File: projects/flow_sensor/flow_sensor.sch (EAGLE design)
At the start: 92 parts, among them IC1 TPS61200, IC2 TPS61200, IC3 MIC5219BM5, J5 455-1750-1-ND

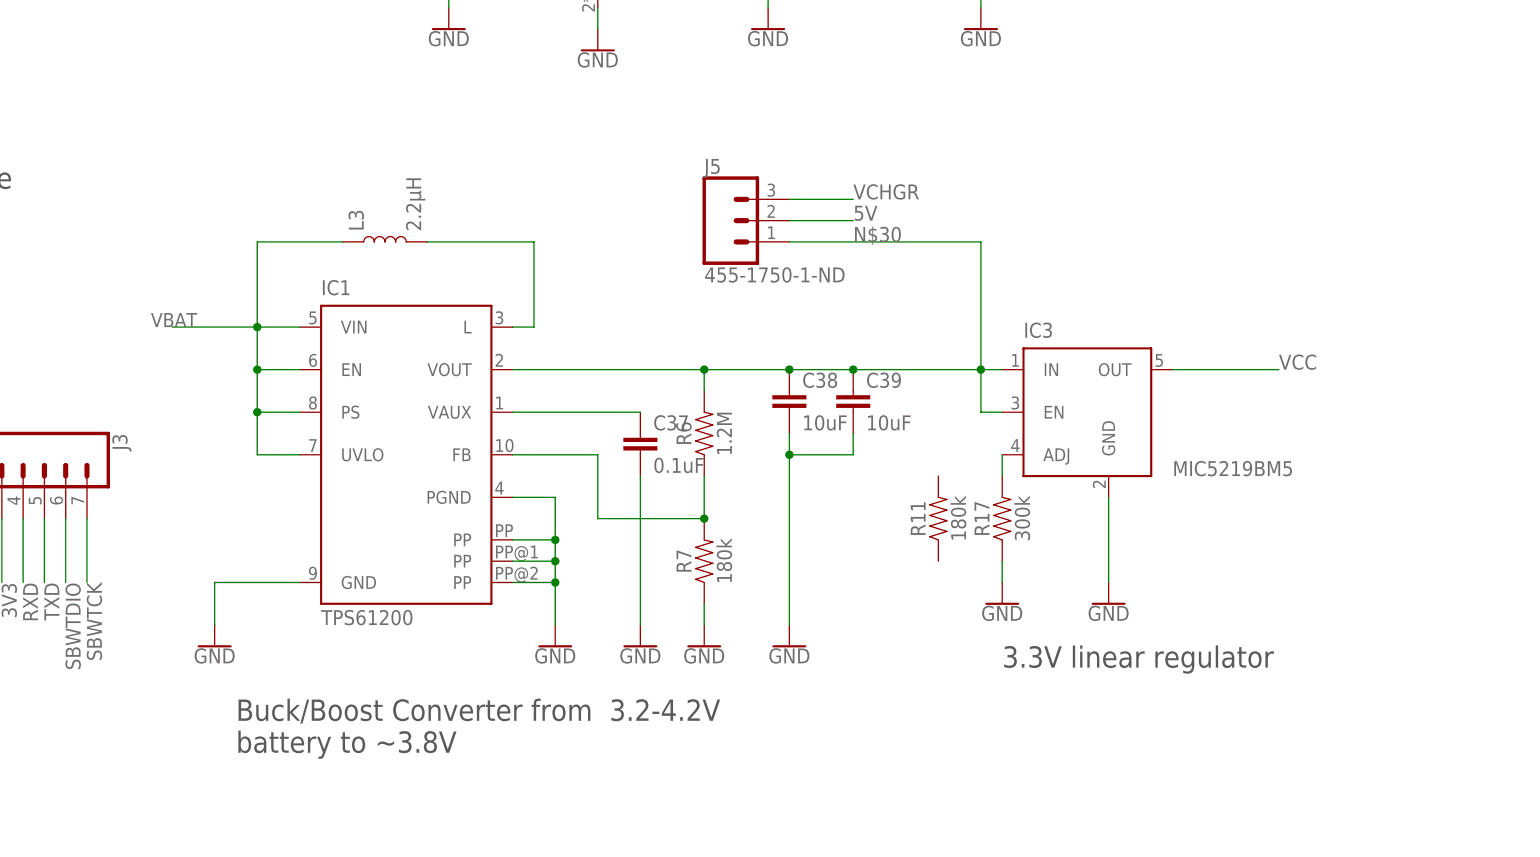
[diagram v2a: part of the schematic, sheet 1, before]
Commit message: Added MAX1726 linear regulator and replaced circuit-side boost converter
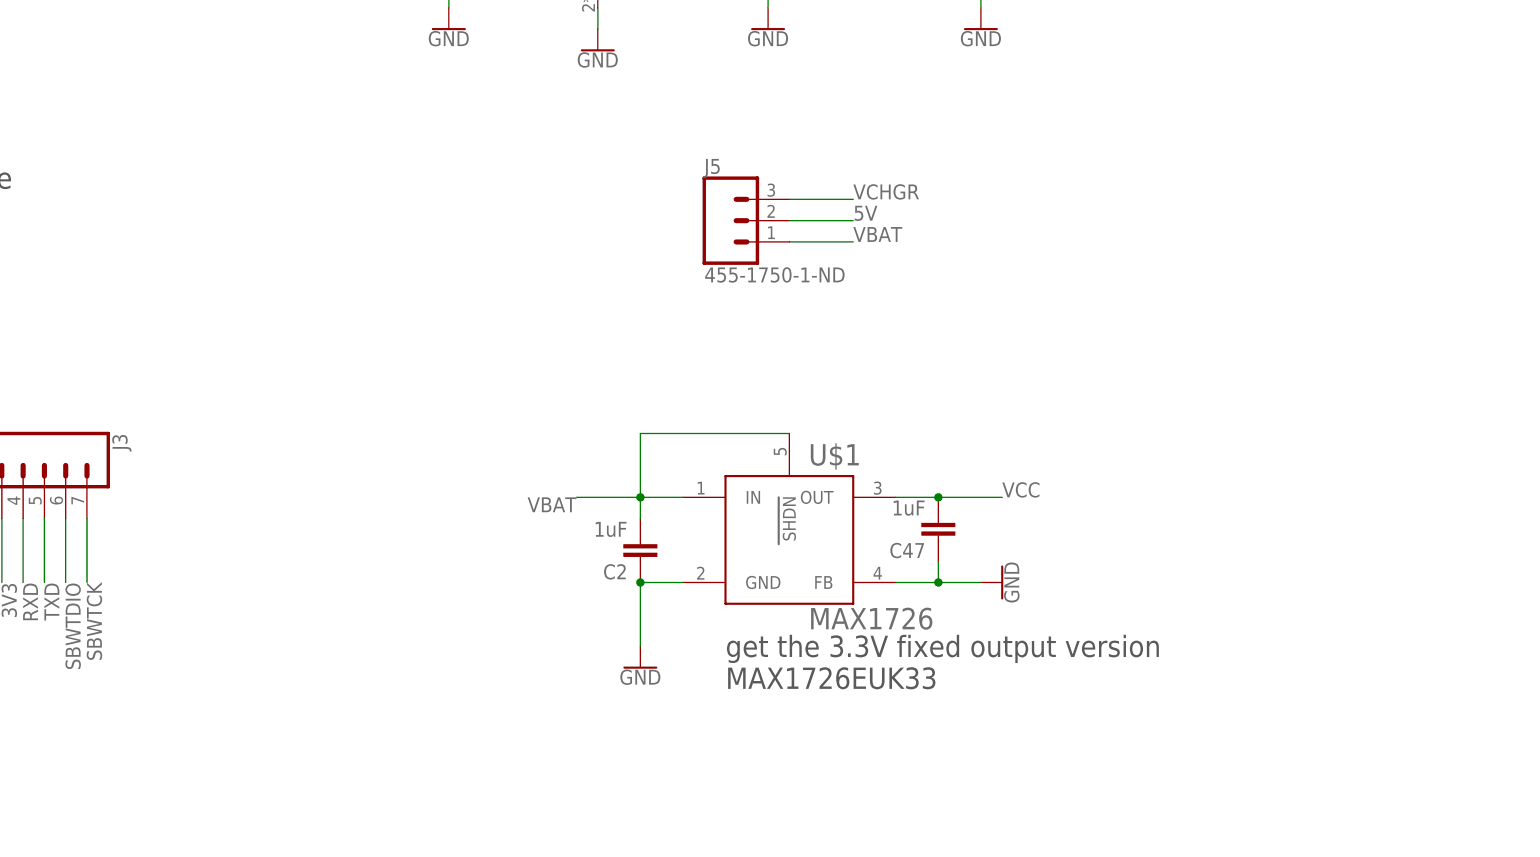
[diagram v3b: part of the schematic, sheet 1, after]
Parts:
- removed C37: 0.1uF, SparkFun-Capacitors:0.1UF-0603-25V-(+80/-20%)
- removed C38, C39: 10uF, SparkFun-Capacitors:10UF-0603-6.3V-20%
- removed IC1: TPS61200, texas:TPS61200
- removed IC3: MIC5219BM5, v-reg-micrel:MIC5219BM5
- removed L3: 2.2µH, SparkFun-Coils:INDUCTOR-0805-3.3UH
- removed R11, R7: 180k, SparkFun-Resistors:180OHM-0603-1/10W-1%
- removed R17: 300k, SparkFun-Resistors:180OHM-0603-1/10W-1%
- removed R6: 1.2M, SparkFun-Resistors:1MOHM-0603-1/4W-5%
- added C2, C47: 1uF, SparkFun-Capacitors:4.7UF0603
- added U$1: MAX1726, my_library:MAX1726
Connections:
- removed net N$17: IC1.FB, R6.1, R7.2
- removed net N$20: IC1.L, L3.2
- removed net N$25: IC3.ADJ, R17.2
- removed net N$3: C37.1, IC1.VAUX
- removed net N$30: C38.1, C39.1, IC1.VOUT, IC3.EN, IC3.IN, J5.1, R6.2
- net GND: now also C2.1, C47.1, U$1.FB, U$1.GND; no longer C37.2, C38.2, C39.2, IC1.GND, IC1.PGND, IC1.PP, IC1.PP@1, IC1.PP@2, IC3.GND, R17.1, R7.1
- net VBAT: now also C2.2, J5.1, U$1.IN, U$1.SHDN; no longer IC1.EN, IC1.PS, IC1.UVLO, IC1.VIN, L3.1
- net VCC: now also C47.2, U$1.OUT; no longer IC3.OUT
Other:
- note added: "get the 3.3V fixed output version MAX1726EUK33"
- note removed: "3.3V linear regulator"
- note removed: "Buck/Boost Converter from 3.2-4.2V battery to ~3.8V"

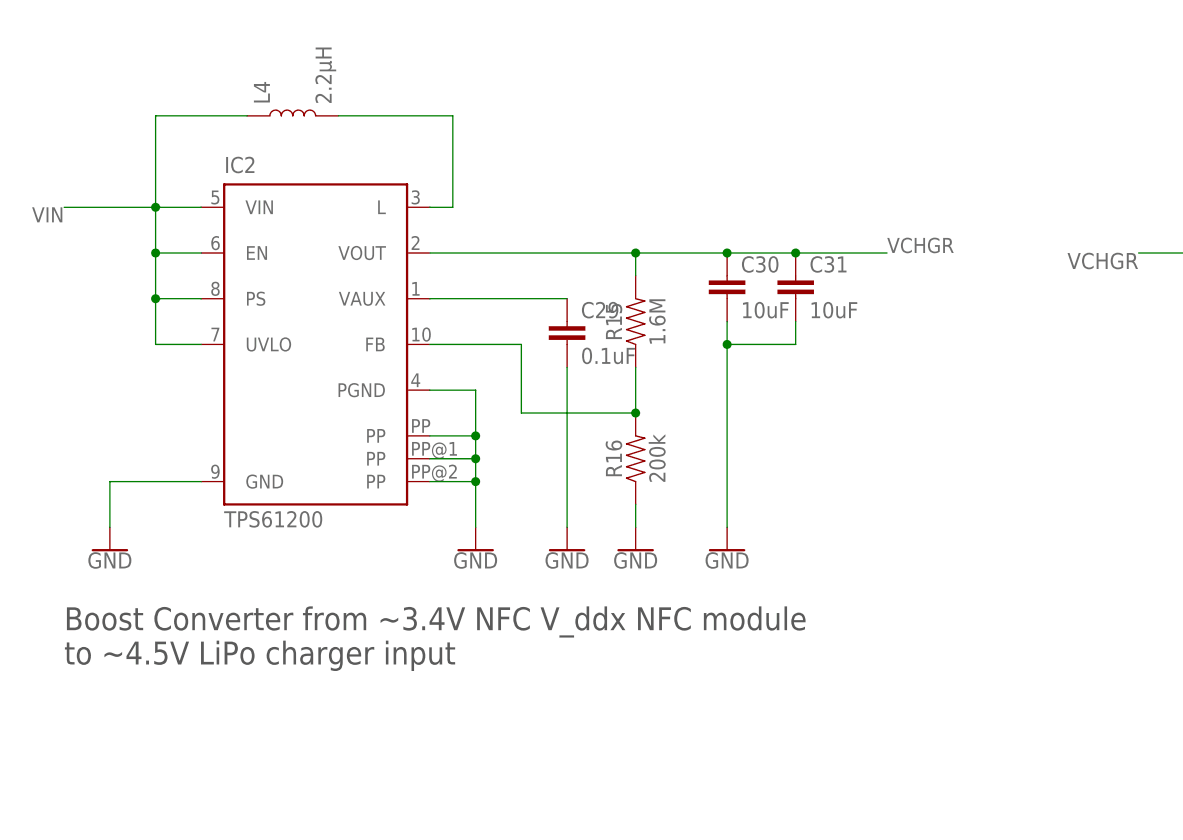
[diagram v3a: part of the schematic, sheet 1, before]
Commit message: Added LTC1517-5 charge pump to replace battery-site boost converter
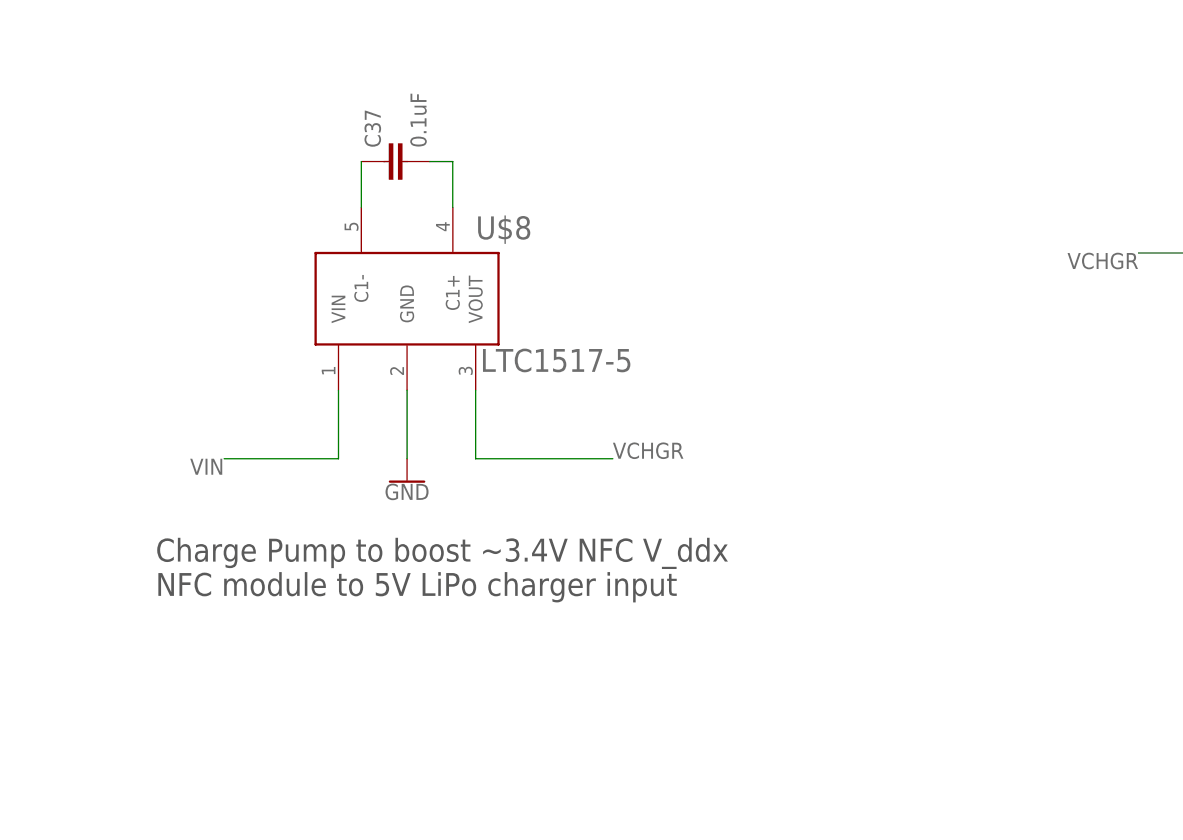
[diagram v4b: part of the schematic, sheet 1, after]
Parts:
- removed C29: 0.1uF, SparkFun-Capacitors:0.1UF-0603-25V-(+80/-20%)
- removed C30, C31: 10uF, SparkFun-Capacitors:10UF-0603-6.3V-20%
- removed IC2: TPS61200, texas:TPS61200
- removed L4: 2.2µH, SparkFun-Coils:INDUCTOR-0805-3.3UH
- removed R15: 1.6M, SparkFun-Resistors:1MOHM-0603-1/4W-5%
- removed R16: 200k, SparkFun-Resistors:180OHM-0603-1/10W-1%
- added C37: 0.1uF, SparkFun-Capacitors:0.1UF-0603-25V-(+80/-20%)
- added U$8: LTC1517-5, my_library:LTC1517-5
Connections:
- removed net N$1: IC2.L, L4.2
- removed net N$18: C29.1, IC2.VAUX
- removed net N$22: IC2.FB, R15.1, R16.2
- new net N$2: C37.1, U$8.C1-
- new net N$3: C37.2, U$8.C1+
- net GND: now also U$8.GND; no longer C29.2, C30.2, C31.2, IC2.GND, IC2.PGND, IC2.PP, IC2.PP@1, IC2.PP@2, R16.1
- net VCHGR: now also U$8.VOUT; no longer C30.1, C31.1, IC2.VOUT, R15.2
- net VIN: now also U$8.VIN; no longer IC2.EN, IC2.PS, IC2.UVLO, IC2.VIN, L4.1
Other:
- note added: "Charge Pump to boost ~3.4V NFC V_ddx NFC module to 5V LiPo charger input"
- note removed: "Boost Converter from ~3.4V NFC V_ddx NFC module to ~4.5V LiPo charger input"

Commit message: Added RM25C256C EEPROM for external data storage
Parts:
- added C29: 0.1uF, SparkFun-Capacitors:0.1UF-0603-25V-(+80/-20%)
- added U$10: RM25C256C, my_library:RM25C256C
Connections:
- removed net SCLK: U$2.DATA_CLK, U$6.SCLK, U$9.(UCB0CLK)P2.2
- new net SCK: U$10.SCK, U$2.DATA_CLK, U$6.SCLK, U$9.(UCB0CLK)P2.2
- net GND: now also C29.2, U$10.GND
- net MISO: now also U$10.SDO
- net MOSI: now also U$10.SDI
- net VCC: now also C29.1, U$10.VCC
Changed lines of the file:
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@@
 <part name="GND17" library="SparkFun-PowerSymbols" deviceset="GND" device=""/>
 <part name="C37" library="SparkFun-Capacitors" deviceset="0.1UF" device="-0603-25V-(+80/-20%)" value="0.1uF"/>
+<part name="U$10" library="my_library" deviceset="RM25C256C" device=""/>
+<part name="C29" library="SparkFun-Capacitors" deviceset="0.1UF" device="-0603-25V-(+80/-20%)" value="0.1uF"/>
+<part name="GND18" library="SparkFun-PowerSymbols" deviceset="GND" device=""/>
 </parts>
 <sheets>
@@
 </segment>
 </net>
-<net name="SCLK" class="0">
+<net name="SCK" class="0">
 <segment>
 <pinref part="U$6" gate="G$1" pin="SCLK"/>
@@
 <instance part="GND42" gate="1" x="203.2" y="5.08"/>
 <instance part="U$3" gate="G$1" x="388.62" y="12.7"/>
+<instance part="U$10" gate="G$1" x="193.04" y="-55.88"/>
+<instance part="C29" gate="G$1" x="190.5" y="-78.74" rot="R90"/>
+<instance part="GND18" gate="1" x="193.04" y="-86.36"/>
 </instances>
 <busses>
@@
 <wire x1="203.2" y1="7.62" x2="203.2" y2="10.16" width="0.1524" layer="91"/>
 </segment>
+<segment>
+<pinref part="GND18" gate="1" pin="GND"/>
+<pinref part="C29" gate="G$1" pin="2"/>
+<wire x1="193.04" y1="-83.82" x2="193.04" y2="-78.74" width="0.1524" layer="91"/>
+<pinref part="U$10" gate="G$1" pin="GND"/>
+<wire x1="190.5" y1="-68.58" x2="193.04" y2="-68.58" width="0.1524" layer="91"/>
+<wire x1="193.04" y1="-68.58" x2="193.04" y2="-78.74" width="0.1524" layer="91"/>
+<junction x="193.04" y="-78.74"/>
+</segment>
 </net>
 <net name="N$5" class="0">
@@
 <pinref part="R24" gate="G$1" pin="2"/>
 </segment>
+<segment>
+<pinref part="U$10" gate="G$1" pin="VCC"/>
+<pinref part="C29" gate="G$1" pin="1"/>
+<wire x1="185.42" y1="-68.58" x2="185.42" y2="-78.74" width="0.1524" layer="91"/>
+<wire x1="185.42" y1="-78.74" x2="185.42" y2="-86.36" width="0.1524" layer="91"/>
+<junction x="185.42" y="-78.74"/>
+<label x="185.42" y="-86.36" size="1.778" layer="95" rot="R270"/>
+</segment>
 </net>
 <net name="N$8" class="0">
@@
 <pinref part="U$9" gate="G$1" pin="(UCB0SDA/UCB0SIMO)P1.6"/>
 </segment>
+<segment>
+<pinref part="U$10" gate="G$1" pin="SDI"/>
+<wire x1="200.66" y1="-43.18" x2="200.66" y2="-35.56" width="0.1524" layer="91"/>
+<label x="200.66" y="-35.56" size="1.778" layer="95" rot="R90"/>
+</segment>
 </net>
 <net name="MISO" class="0">
@@
 <label x="-132.08" y="53.34" size="1.6764" layer="95" rot="R90"/>
 </segment>
-</net>
-<net name="SCLK" class="0">
-<segment>
-<pinref part="U$2" gate="G$1" pin="DATA_CLK"/>
-<wire x1="-86.36" y1="43.18" x2="-121.92" y2="43.18" width="0.1524" layer="91"/>
-<wire x1="-121.92" y1="43.18" x2="-121.92" y2="53.34" width="0.1524" layer="91"/>
-<label x="-121.92" y="53.34" size="1.6764" layer="95" rot="R90"/>
-</segment>
-<segment>
-<wire x1="317.5" y1="10.16" x2="325.12" y2="10.16" width="0.1524" layer="91"/>
-<label x="325.12" y="10.16" size="1.778" layer="95"/>
-<pinref part="U$9" gate="G$1" pin="(UCB0CLK)P2.2"/>
+<segment>
+<pinref part="U$10" gate="G$1" pin="SDO"/>
+<wire x1="198.12" y1="-43.18" x2="198.12" y2="-35.56" width="0.1524" layer="91"/>
+<label x="198.12" y="-35.56" size="1.778" layer="95" rot="R90"/>
 </segment>
 </net>
@@
 </segment>
 </net>
+<net name="SCK" class="0">
+<segment>
+<pinref part="U$10" gate="G$1" pin="SCK"/>
+<wire x1="195.58" y1="-43.18" x2="195.58" y2="-35.56" width="0.1524" layer="91"/>
+<label x="195.58" y="-35.56" size="1.778" layer="95" rot="R90"/>
+</segment>
+<segment>
+<pinref part="U$2" gate="G$1" pin="DATA_CLK"/>
+<wire x1="-86.36" y1="43.18" x2="-121.92" y2="43.18" width="0.1524" layer="91"/>
+<wire x1="-121.92" y1="43.18" x2="-121.92" y2="53.34" width="0.1524" layer="91"/>
+<label x="-121.92" y="53.34" size="1.6764" layer="95" rot="R90"/>
+</segment>
+<segment>
+<wire x1="317.5" y1="10.16" x2="325.12" y2="10.16" width="0.1524" layer="91"/>
+<label x="325.12" y="10.16" size="1.778" layer="95"/>
+<pinref part="U$9" gate="G$1" pin="(UCB0CLK)P2.2"/>
+</segment>
+</net>

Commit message: Beginning v2.0 routing
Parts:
- removed C44: 2.2n, SparkFun-Capacitors:1.0UF-0603-16V-10%
- removed J4: (no value), SparkFun-Connectors:CONN_021X02_NO_SILK
- removed R24: 47k, SparkFun-Resistors:680OHM-0603-1/10W-5%
- removed R4, R5: 10k, SparkFun-Resistors:10KOHM-0603-1/10W-1%
- removed U$9: MSP430FR5994, my_library:MSP430FR5994
- added C30: 2.2n, SparkFun-Capacitors:1.0UF-0603-16V-10%
- added C31, C48: 1.0uF, SparkFun-Capacitors:1.0UF-0603-16V-10%
- added C38, C39: 0.1uF, SparkFun-Capacitors:0.1UF-0603-25V-(+80/-20%)
- added R1: 47k, SparkFun-Resistors:680OHM-0603-1/10W-5%
- added R11, R6, R7: 10k, SparkFun-Resistors:10KOHM-0603-1/10W-1%
- C27: value 1.0uF -> 3.3uF; device SparkFun-Capacitors:1.0UF-0603-16V-10% -> SparkFun-Capacitors:0.1UF-0603-25V-(+80/-20%)
- C29: value 0.1uF -> 1uF
- C40: value 0.1uF -> 10uF
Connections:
- removed net COMMS_EN2: R3.1, U$2.EN2, U$9.P3.6
- removed net N$28: J4.2, U$4.-IN1
- removed net N$35: R22.2, U$9.(A9)P4.1
- removed net N$5: R4.2, U$2.I/O_1
- removed net N$7: R5.2, U$2.I/O_2
- new net 3.3V: R11.1, R7.1
- new net BRIDGE_VCC: R3.2, R6.2
- new net MEM_SS: U$10.CS
- new net N$1: R22.2
- new net N$18: R6.1, R7.2, U$4.-IN1
- net CHG_STAT: no longer U$9.P3.4
- net COMMS_EN: no longer U$9.P3.5
- net COMMS_IRQ: no longer U$9.P3.7
- net COMMS_SS: no longer U$9.P4.5
- net GND: now also C27.2, C30.1, C31.1, C38.1, C39.1, C40.2, C48.1, U$3.14, U$3.19, U$3.49, U$3.68; no longer C27.1, C40.1, C44.1, R3.2, U$9.AVSS1, U$9.AVSS2, U$9.AVSS3, U$9.DVSS1
- net MISO: no longer U$9.(UCB0SCL/UCB0SOMI)P1.7
- net MOSI: no longer U$9.(UCB0SDA/UCB0SIMO)P1.6
- net N$29: now also R11.2, R3.1; no longer J4.1
- net N$34: no longer U$9.(A8)P4.0
- net N$38: no longer U$9.(A10)P4.2
- net RXD: now also U$3.41; no longer U$9.(UCA0RXD/UCA0SOMI)P2.1
- net SBWTCK: now also U$3.71; no longer U$9.SBWTCK
- net SBWTDIO: now also C30.2, R1.1, U$3.76; no longer C44.2, R24.1, U$9.~RESET(SBWTDIO)
- net SCK: no longer U$9.(UCB0CLK)P2.2
- net SENSOR_OUT: no longer U$9.(A2)P1.2
- net TEMP_SS: no longer U$9.P4.6
- net TXD: now also U$3.40; no longer U$9.(UCA0TXD/UCA0SIMO)P2.0
- net VCC: now also C31.2, C38.2, C39.2, C48.2, R1.2, U$2.EN2, U$3.11, U$3.18, U$3.50; no longer C27.2, C40.2, R24.2, U$9.AVCC1, U$9.DVCC1
- net VCHGR: now also C40.1
- net VIN: now also C27.1, U$2.I/O_1, U$2.I/O_2; no longer R4.1, R5.1
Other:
- moved on the sheet: C25, C26, D1, D2, D3, R21, R22, R23, U$3
